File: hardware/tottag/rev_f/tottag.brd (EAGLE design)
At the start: 61 x 34.5 mm, 148 parts, among them J1 MICRO_USB_B_HIROSE_ZX62-B-5PA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, J2 CON_MICRO_SDDM3AT-SF-PEJM5, J3 BAT_HOLE, J4 TC2030-JLINK-NL, J5 TC2030-JLINK-NL, T1 HHM1595A1, U1 DW1000, U10 STM32F091CC, U2 FT232RQ, U3 LIS2DW12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

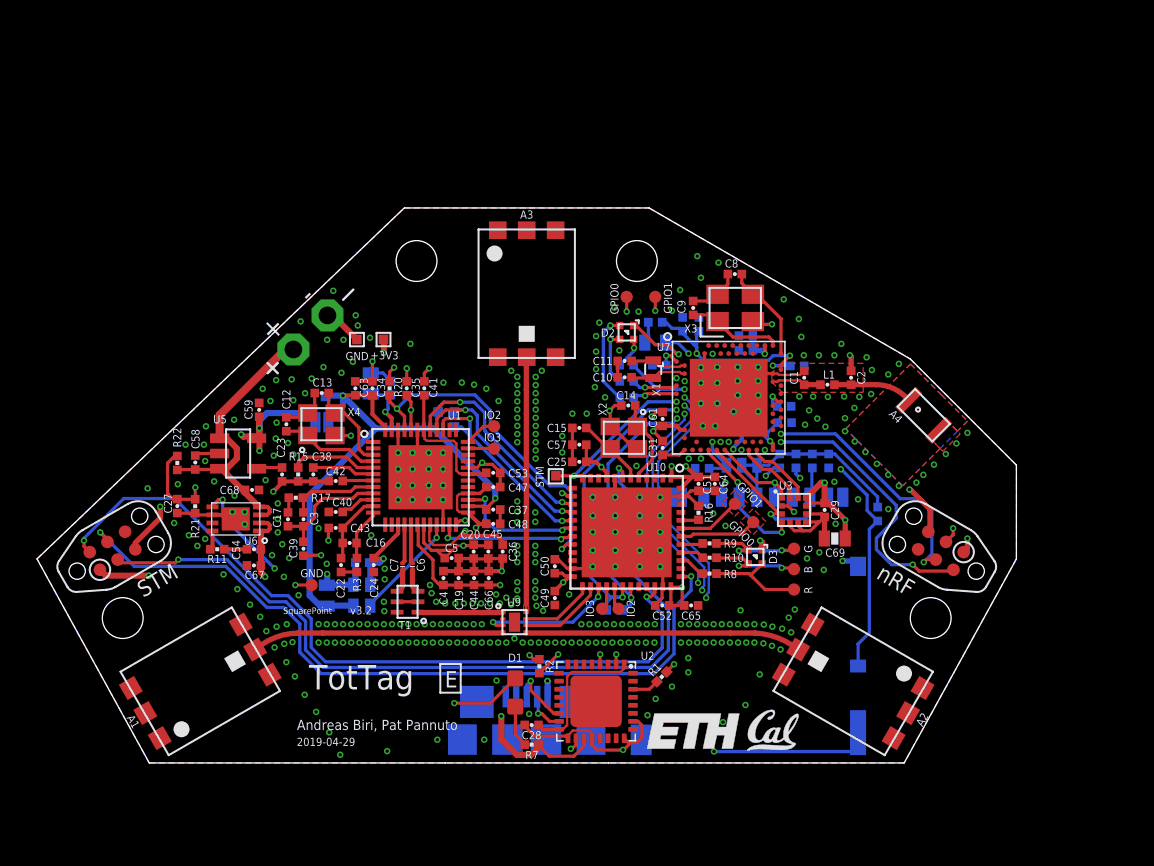
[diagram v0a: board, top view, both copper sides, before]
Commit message: added RTC to schematic; supply battery still missing
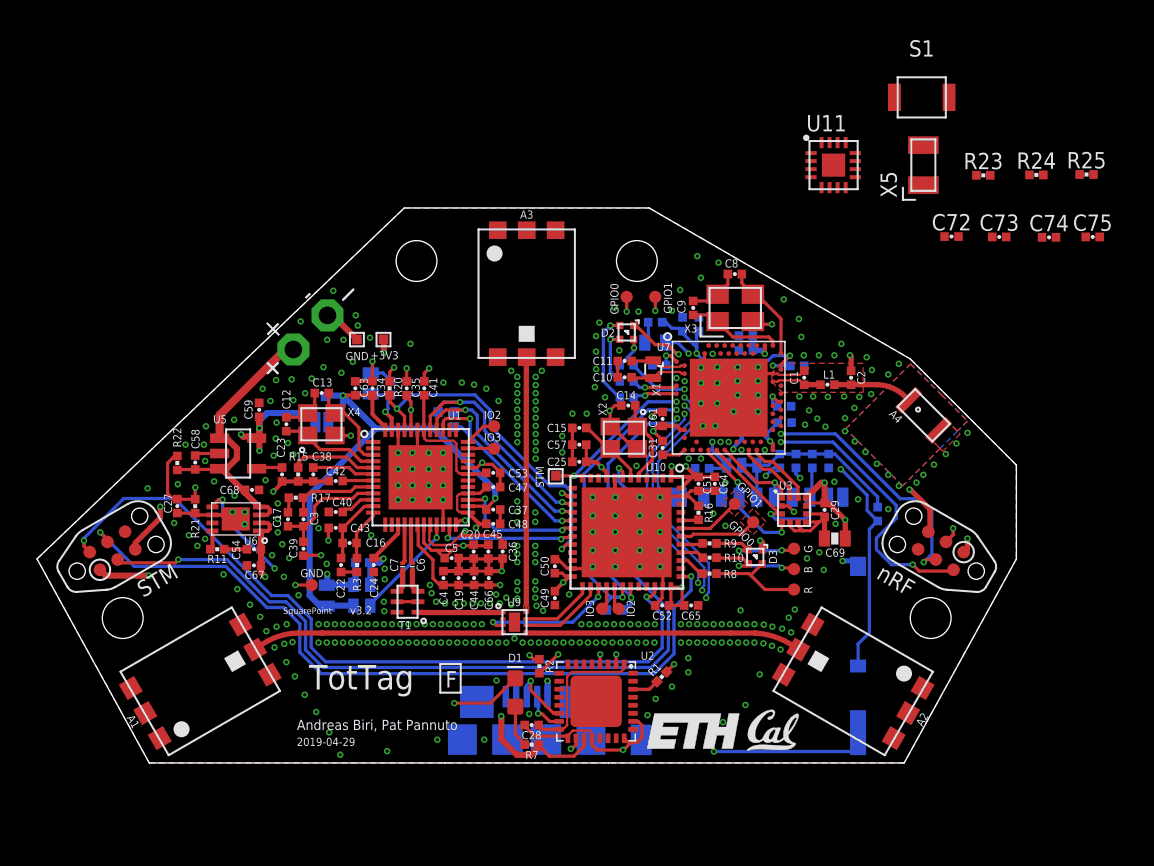
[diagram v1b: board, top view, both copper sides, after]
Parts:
- added C72: 47pF, passives:0402_CAP
- added C73: 1uF, passives:0402_CAP
- added C74, C75: DNP, passives:0402_CAP
- added R23, R24, R25: 10k, passives:0402_RES
- added S1: B3U-1000P, switches:B3U-1000P
- added U11: AB1815-T3, chips:QFN-16-3MM
- added X5: ABS07-32.768KHZ-7-T, crystals:2-SMD
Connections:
- new net !NRF_CS_RTC: U11.12, U7.B11
- new net !RTC_EXTR: R23.1, S1.2, U11.3
- new net !RTC_IRQ: U11.11, U7.A10
- new net N$35: C72.1, U11.14
- new net N$41: C75.1, U11.16, X5.1
- new net N$42: C74.1, U11.15, X5.2
- new net RTC_WDI: R25.1, U11.2, U7.A12
- new net VBAT_RTC: U11.5
- new net VCC: C73.1, R23.2, R24.2, R25.2, U11.13
- net !NRF_RST: now also R24.1, U11.1
- net GND: now also C72.2, C73.2, C74.2, C75.2, S1.1, U11.GND
- net NRF_MISO: now also U11.6
- net NRF_MOSI: now also U11.9
- net NRF_SCK: now also U11.7
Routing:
- net GND: track 165.3 -> 164.7 mm
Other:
- board text added: "F"
- board text removed: "E"

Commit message: added battery, fixed RTC passives
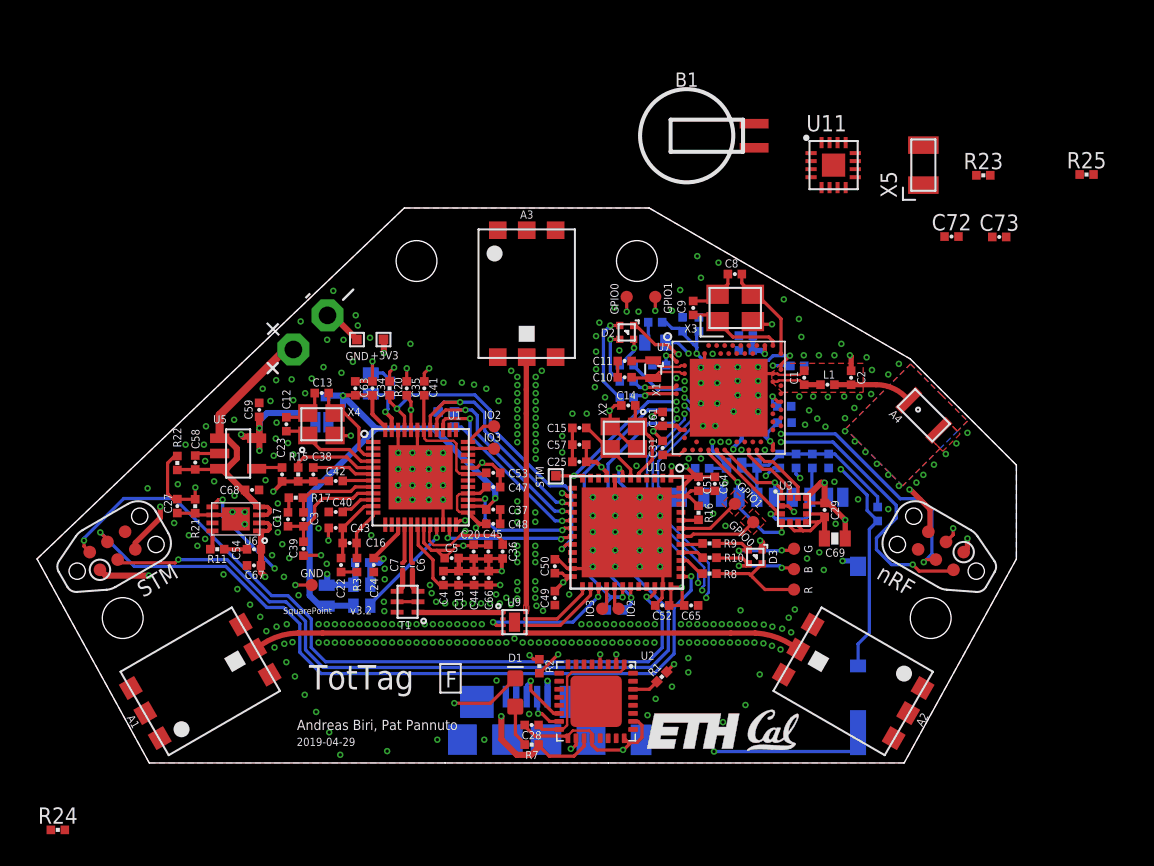
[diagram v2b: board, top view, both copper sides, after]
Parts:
- removed C74, C75: DNP, passives:0402_CAP
- removed S1: B3U-1000P, switches:B3U-1000P
- added B1: (no value), batteries:MS518SE-FL35E
- R24: value 10k -> 1.41k
- moved R24 73.3 mm to (-29.2, -7.98)
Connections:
- removed net !RTC_EXTR: R23.1, S1.2, U11.3
- new net N$43: R23.1, U11.10
- new net N$45: B1.+, R24.2
- net !NRF_RST: no longer R24.1, U11.1
- net GND: now also B1.-, U11.3; no longer C74.2, C75.2, S1.1
- net N$41: no longer C75.1
- net N$42: no longer C74.1
- net VBAT_RTC: now also R23.2, R24.1, R25.2
- net VCC: no longer R23.2, R24.2, R25.2

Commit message: add pull-up for CS to prevent floating if nRF is turned off
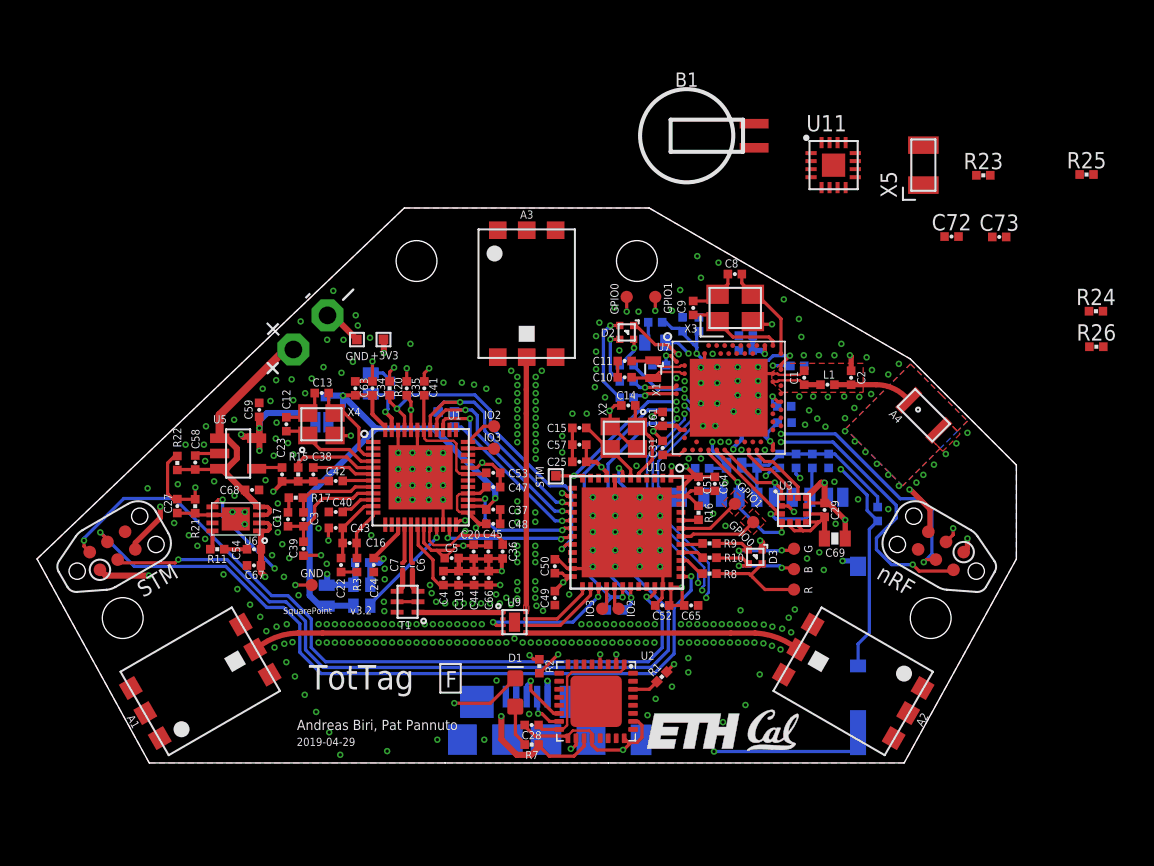
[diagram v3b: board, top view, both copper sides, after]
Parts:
- added R26: 10k, passives:0402_RES
- moved R24 72.2 mm to (35.4, 24.3)
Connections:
- net !NRF_CS_RTC: now also R26.1
- net VBAT_RTC: now also R26.2
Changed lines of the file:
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@@
 <attribute name="NAME" x="9.9568" y="38.2778" size="0.889" layer="25" font="vector" ratio="12" align="bottom-center"/>
 </element>
-<element name="R24" library="passives" package="0402_RES" value="1.41k" x="-29.1846" y="-7.9756" smashed="yes">
-<attribute name="DIGIKEY" value="311-10KJRCT-ND " x="-27.7876" y="-7.9756" size="1.778" layer="27" display="off"/>
-<attribute name="MPN" value="RC0402JR-0710KL" x="-27.7876" y="-7.9756" size="1.778" layer="27" display="off"/>
-<attribute name="NAME" x="-29.1846" y="-7.5946" size="1.016" layer="25" font="vector" ratio="12" align="bottom-center"/>
-<attribute name="VALUE" x="-29.1846" y="-9.3726" size="1.016" layer="27" font="vector" ratio="12" align="bottom-center"/>
+<element name="R24" library="passives" package="0402_RES" value="1.41k" x="35.433" y="24.3078" smashed="yes">
+<attribute name="DIGIKEY" value="311-10KJRCT-ND " x="36.83" y="24.3078" size="1.778" layer="27" display="off"/>
+<attribute name="MPN" value="RC0402JR-0710KL" x="36.83" y="24.3078" size="1.778" layer="27" display="off"/>
+<attribute name="NAME" x="35.433" y="24.6888" size="1.016" layer="25" font="vector" ratio="12" align="bottom-center"/>
+<attribute name="VALUE" x="35.433" y="22.9108" size="1.016" layer="27" font="vector" ratio="12" align="bottom-center"/>
+</element>
+<element name="R26" library="passives" package="0402_RES" value="10k" x="35.4584" y="22.098" smashed="yes">
+<attribute name="DIGIKEY" value="311-10KJRCT-ND " x="35.4584" y="22.098" size="1.778" layer="27" display="off"/>
+<attribute name="MPN" value="RC0402JR-0710KL" x="35.4584" y="22.098" size="1.778" layer="27" display="off"/>
+<attribute name="NAME" x="35.4584" y="22.479" size="1.016" layer="25" font="vector" ratio="12" align="bottom-center"/>
+<attribute name="VALUE" x="35.4584" y="20.701" size="1.016" layer="27" font="vector" ratio="12" align="bottom-center"/>
 </element>
 </elements>
@@
 <contactref element="U11" pad="12"/>
 <contactref element="U7" pad="B11"/>
+<contactref element="R26" pad="1"/>
 <wire x1="12.073" y1="21.673" x2="20.4508" y2="34.151" width="0" layer="19" extent="1-1"/>
+<wire x1="35.02533125" y1="22.098" x2="12.073" y2="21.673" width="0" layer="19" extent="1-1"/>
 </signal>
 <signal name="VBAT_RTC">
@@
 <contactref element="R25" pad="2"/>
 <contactref element="R24" pad="1"/>
+<contactref element="R26" pad="2"/>
 <wire x1="28.85566875" y1="32.766" x2="35.28186875" y2="32.8168" width="0" layer="19" extent="1-1"/>
 <wire x1="18.3508" y1="32.001" x2="28.85566875" y2="32.766" width="0" layer="19" extent="1-1"/>
-<wire x1="-29.61766875" y1="-7.9756" x2="18.3508" y2="32.001" width="0" layer="19" extent="1-1"/>
+<wire x1="34.99993125" y1="24.3078" x2="18.3508" y2="32.001" width="0" layer="19" extent="1-1"/>
+<wire x1="35.89146875" y1="22.098" x2="34.99993125" y2="24.3078" width="0" layer="19" extent="1-1"/>
 </signal>
 <signal name="N$43">
@@
 <contactref element="R24" pad="2"/>
 <contactref element="B1" pad="+"/>
-<wire x1="-28.75153125" y1="-7.9756" x2="14.1568" y2="35.9798" width="0" layer="19" extent="1-1"/>
+<wire x1="35.86606875" y1="24.3078" x2="14.1568" y2="35.9798" width="0" layer="19" extent="1-1"/>
 </signal>
 </signals>

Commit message: added layout
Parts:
- moved R26 22.9 mm to (13.5, 28.4), flipped to the bottom
- moved R24 22.5 mm to (13.5, 29.5), flipped to the bottom, turned to 180 degrees
- moved R25 22.1 mm to (13.5, 27.3), flipped to the bottom
- moved R23 16.2 mm to (13.5, 26.3), flipped to the bottom
- moved B1 13.6 mm to (19.5, 25.5), flipped to the bottom, turned to 40 degrees
- moved C73 10.3 mm to (21.9, 21.8), turned to 270 degrees
- moved U11 9.02 mm to (19.1, 24.4), turned to 270 degrees
- moved X5 8.61 mm to (22.6, 25.0), turned to 270 degrees
- moved C72 8.03 mm to (22.8, 21.8), turned to 270 degrees
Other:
- outline, holes or cut-outs redrawn

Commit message: routing finished; hardware revision F ready for review
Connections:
- net !NRF_CS_RTC: now also U7.A10; no longer U7.B11
- net !RTC_IRQ: now also U7.A12; no longer U7.A10
- net RTC_WDI: now also U7.A8; no longer U7.A12
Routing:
- net !NRF_CS_RTC: track 0.00 -> 21.6 mm, vias 0 -> 2
- net NRF_MISO: track 12.1 -> 28.7 mm, vias 1 -> 2
- net RTC_WDI: track 0.00 -> 15.4 mm, vias 0 -> 2
- net NRF_SCK: track 6.02 -> 20.3 mm, vias 1 -> 2
- net NRF_MOSI: track 11.3 -> 24.0 mm, vias 3 -> 4
- net !RTC_IRQ: track 0.00 -> 9.36 mm, vias 0 -> 2
- net N$43: track 0.00 -> 8.69 mm, vias 0 -> 1
- net VBAT_RTC: track 0.00 -> 8.34 mm, vias 0 -> 1
- net N$35: track 0.00 -> 3.56 mm
- net N$45: track 0.00 -> 3.10 mm
- net N$41: track 0.00 -> 2.56 mm
- net N$42: track 0.00 -> 2.43 mm
- net GND: track 164.7 -> 167.1 mm, vias 386 -> 406
- net VCC: track 0.00 -> 2.26 mm
- net N$9: track 11.5 -> 12.7 mm

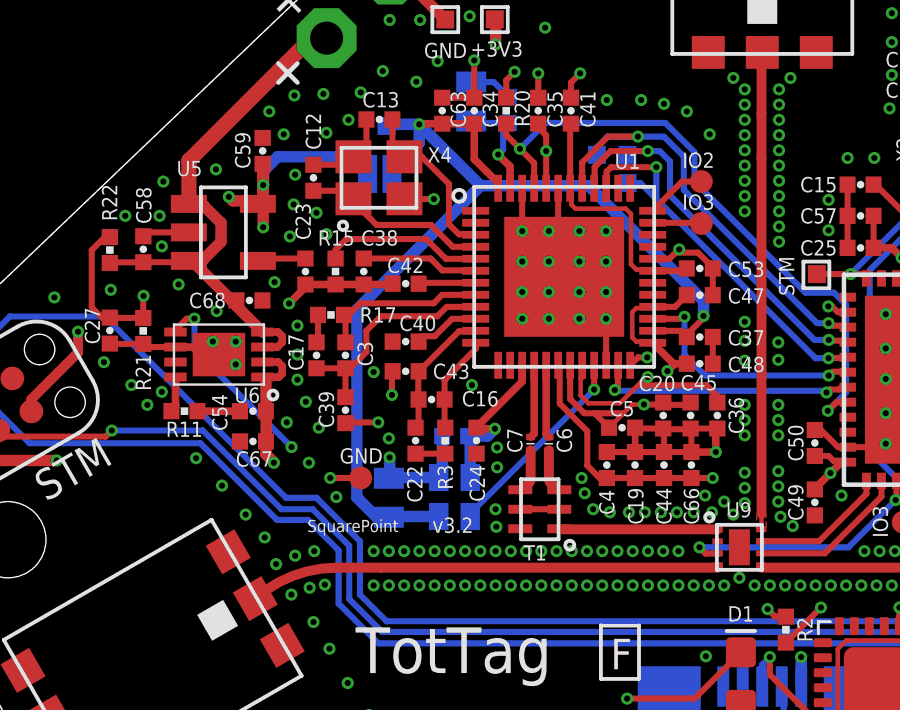
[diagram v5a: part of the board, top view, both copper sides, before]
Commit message: Replace obsolete power regulator
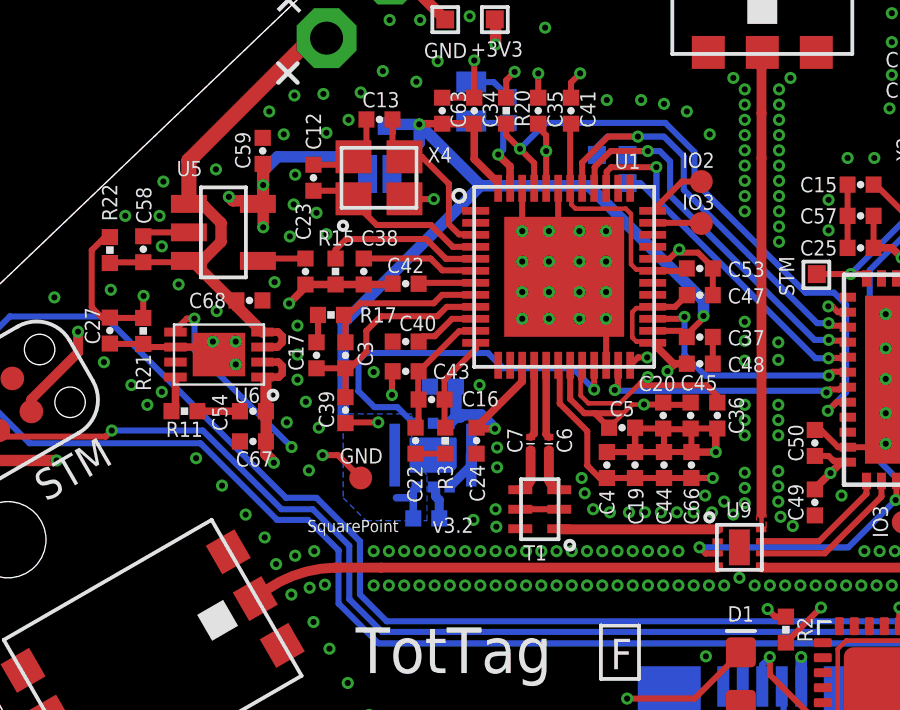
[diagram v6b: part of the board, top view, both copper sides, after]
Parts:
- C70: device passives:0603_CAP -> passives:0402_CAP
- U4: value LXDC2HN18A -> XCL206B"; device regulators:LXDC2HN -> regulators:XCL20X
- moved C62 1.70 mm to (-10.6, 10.3), turned to 0 degrees
- moved U4 1.57 mm to (-11.0, 8.03)
- moved C70 1.42 mm to (-11.2, 5.92), turned to 180 degrees
- moved U$1 1.27 mm to (-14.5, 9.65)
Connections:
- new net N$44: U4.1, U4.7
- net +1V8: now also U4.8
- net +3V3: now also C62.1, U4.6; no longer C62.2, U4.1
- net GND: now also C62.2, U4.2, U4.5; no longer C62.1, U4.4
- net REG_EN: now also U4.4; no longer U4.2
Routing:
- net REG_EN: track 6.75 -> 12.7 mm
- net +1V8: track 37.2 -> 33.5 mm
- net GND: track 167.1 -> 165.0 mm, vias 406 -> 404
- net N$44: track 0.00 -> 1.36 mm
- added copper zone on layer 16, net +1V8
